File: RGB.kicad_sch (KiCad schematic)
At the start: 36 parts

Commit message: Made the project portable
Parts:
- CRGB1, CRGB10, CRGB11, CRGB12, CRGB13, CRGB14, CRGB15, CRGB16, CRGB17, CRGB18, CRGB2, CRGB3, CRGB4, CRGB5, CRGB6, CRGB7, CRGB8, CRGB9: footprint locallib:C_0603 -> KBD8X_MK2_Components:C_0603; symbol Device:C_Small -> KBD8X_MK2_Components:C_Small
- RGB1, RGB10, RGB11, RGB12, RGB13, RGB14, RGB15, RGB16, RGB17, RGB18, RGB2, RGB3, RGB4, RGB5, RGB6, RGB7, RGB8, RGB9: footprint locallib:LED_WS2812B-PLCC4 -> LED_SMD:LED_WS2812B_PLCC4_5.0x5.0mm_P3.2mm; symbol LED:WS2812B -> KBD8X_MK2_Components:WS2812B

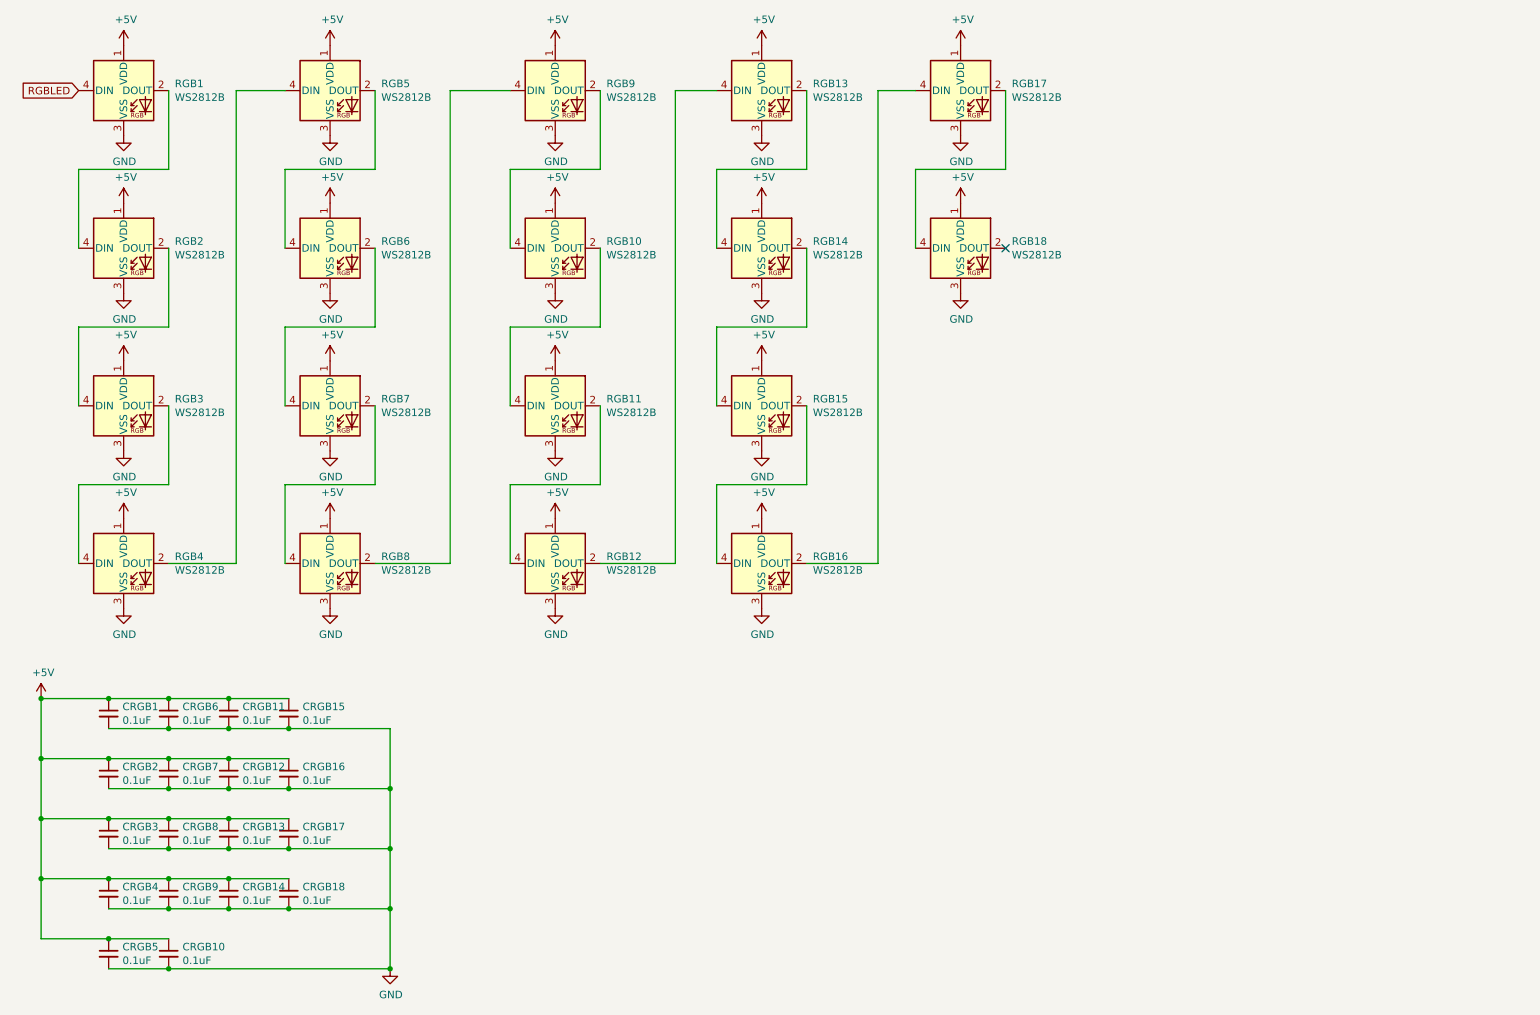
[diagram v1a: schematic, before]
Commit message: Rearrenged schematics items
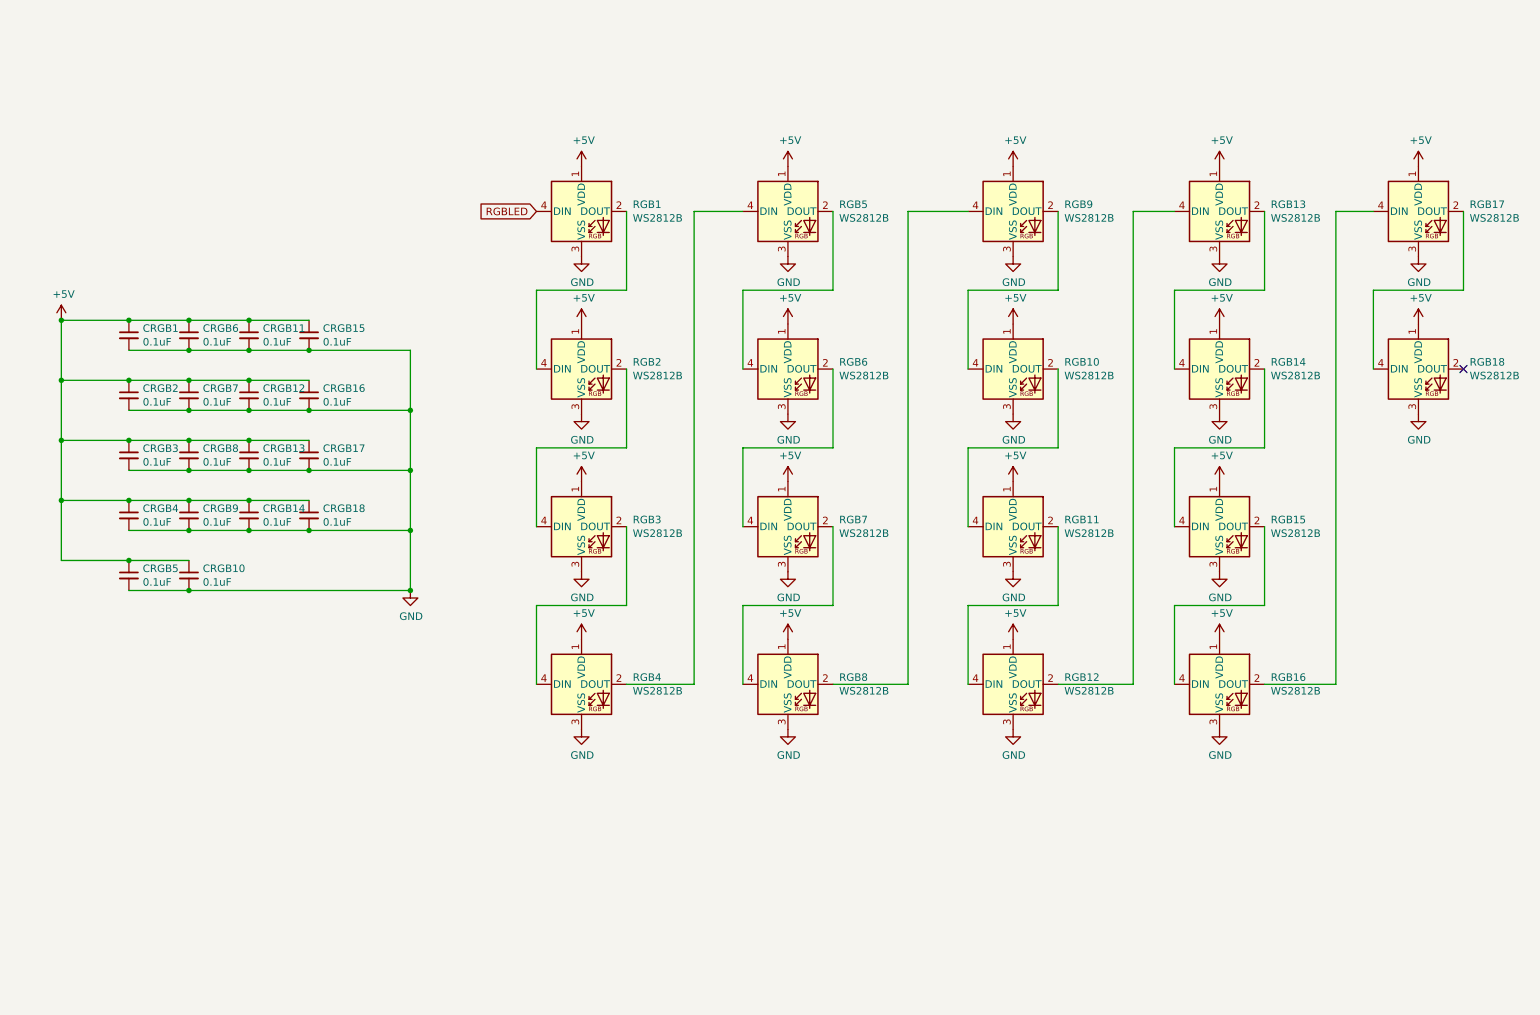
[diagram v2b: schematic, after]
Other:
- moved on the sheet: CRGB1, CRGB10, CRGB11, CRGB12, CRGB13, CRGB14, CRGB15, CRGB16, CRGB17, CRGB18, CRGB2, CRGB3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

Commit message: Added 3U and 10U footprints to the PCB
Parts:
- RGB1, RGB10, RGB11, RGB12, RGB13, RGB14, RGB15, RGB16, RGB17, RGB18, RGB2, RGB3, RGB4, RGB5, RGB6, RGB7, RGB8, RGB9: footprint LED_SMD:LED_WS2812B_PLCC4_5.0x5.0mm_P3.2mm -> KBD8X_MK2_Components:LED_WS2812B-PLCC4
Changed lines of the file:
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@@
       (effects (font (size 1.27 1.27)) (justify left))
     )
-    (property "Footprint" "LED_SMD:LED_WS2812B_PLCC4_5.0x5.0mm_P3.2mm" (id 2) (at 114.935 63.627 0)
+    (property "Footprint" "KBD8X_MK2_Components:LED_WS2812B-PLCC4" (id 2) (at 114.935 63.627 0)
       (effects (font (size 1.27 1.27)) (justify left top) hide)
     )
@@
       (effects (font (size 1.27 1.27)) (justify left))
     )
-    (property "Footprint" "LED_SMD:LED_WS2812B_PLCC4_5.0x5.0mm_P3.2mm" (id 2) (at 114.935 90.297 0)
+    (property "Footprint" "KBD8X_MK2_Components:LED_WS2812B-PLCC4" (id 2) (at 114.935 90.297 0)
       (effects (font (size 1.27 1.27)) (justify left top) hide)
     )
@@
       (effects (font (size 1.27 1.27)) (justify left))
     )
-    (property "Footprint" "LED_SMD:LED_WS2812B_PLCC4_5.0x5.0mm_P3.2mm" (id 2) (at 114.935 116.967 0)
+    (property "Footprint" "KBD8X_MK2_Components:LED_WS2812B-PLCC4" (id 2) (at 114.935 116.967 0)
       (effects (font (size 1.27 1.27)) (justify left top) hide)
     )
@@
       (effects (font (size 1.27 1.27)) (justify left))
     )
-    (property "Footprint" "LED_SMD:LED_WS2812B_PLCC4_5.0x5.0mm_P3.2mm" (id 2) (at 114.935 143.637 0)
+    (property "Footprint" "KBD8X_MK2_Components:LED_WS2812B-PLCC4" (id 2) (at 114.935 143.637 0)
       (effects (font (size 1.27 1.27)) (justify left top) hide)
     )
@@
       (effects (font (size 1.27 1.27)) (justify left))
     )
-    (property "Footprint" "LED_SMD:LED_WS2812B_PLCC4_5.0x5.0mm_P3.2mm" (id 2) (at 149.86 63.627 0)
+    (property "Footprint" "KBD8X_MK2_Components:LED_WS2812B-PLCC4" (id 2) (at 149.86 63.627 0)
       (effects (font (size 1.27 1.27)) (justify left top) hide)
     )
@@
       (effects (font (size 1.27 1.27)) (justify left))
     )
-    (property "Footprint" "LED_SMD:LED_WS2812B_PLCC4_5.0x5.0mm_P3.2mm" (id 2) (at 149.86 90.297 0)
+    (property "Footprint" "KBD8X_MK2_Components:LED_WS2812B-PLCC4" (id 2) (at 149.86 90.297 0)
       (effects (font (size 1.27 1.27)) (justify left top) hide)
     )
@@
       (effects (font (size 1.27 1.27)) (justify left))
     )
-    (property "Footprint" "LED_SMD:LED_WS2812B_PLCC4_5.0x5.0mm_P3.2mm" (id 2) (at 149.86 116.967 0)
+    (property "Footprint" "KBD8X_MK2_Components:LED_WS2812B-PLCC4" (id 2) (at 149.86 116.967 0)
       (effects (font (size 1.27 1.27)) (justify left top) hide)
     )
@@
       (effects (font (size 1.27 1.27)) (justify left))
     )
-    (property "Footprint" "LED_SMD:LED_WS2812B_PLCC4_5.0x5.0mm_P3.2mm" (id 2) (at 149.86 143.637 0)
+    (property "Footprint" "KBD8X_MK2_Components:LED_WS2812B-PLCC4" (id 2) (at 149.86 143.637 0)
       (effects (font (size 1.27 1.27)) (justify left top) hide)
     )
@@
       (effects (font (size 1.27 1.27)) (justify left))
     )
-    (property "Footprint" "LED_SMD:LED_WS2812B_PLCC4_5.0x5.0mm_P3.2mm" (id 2) (at 187.96 63.627 0)
+    (property "Footprint" "KBD8X_MK2_Components:LED_WS2812B-PLCC4" (id 2) (at 187.96 63.627 0)
       (effects (font (size 1.27 1.27)) (justify left top) hide)
     )
@@
       (effects (font (size 1.27 1.27)) (justify left))
     )
-    (property "Footprint" "LED_SMD:LED_WS2812B_PLCC4_5.0x5.0mm_P3.2mm" (id 2) (at 187.96 90.297 0)
+    (property "Footprint" "KBD8X_MK2_Components:LED_WS2812B-PLCC4" (id 2) (at 187.96 90.297 0)
       (effects (font (size 1.27 1.27)) (justify left top) hide)
     )
@@
       (effects (font (size 1.27 1.27)) (justify left))
     )
-    (property "Footprint" "LED_SMD:LED_WS2812B_PLCC4_5.0x5.0mm_P3.2mm" (id 2) (at 187.96 116.967 0)
+    (property "Footprint" "KBD8X_MK2_Components:LED_WS2812B-PLCC4" (id 2) (at 187.96 116.967 0)
       (effects (font (size 1.27 1.27)) (justify left top) hide)
     )
@@
       (effects (font (size 1.27 1.27)) (justify left))
     )
-    (property "Footprint" "LED_SMD:LED_WS2812B_PLCC4_5.0x5.0mm_P3.2mm" (id 2) (at 187.96 143.637 0)
+    (property "Footprint" "KBD8X_MK2_Components:LED_WS2812B-PLCC4" (id 2) (at 187.96 143.637 0)
       (effects (font (size 1.27 1.27)) (justify left top) hide)
     )
@@
       (effects (font (size 1.27 1.27)) (justify left))
     )
-    (property "Footprint" "LED_SMD:LED_WS2812B_PLCC4_5.0x5.0mm_P3.2mm" (id 2) (at 222.885 63.627 0)
+    (property "Footprint" "KBD8X_MK2_Components:LED_WS2812B-PLCC4" (id 2) (at 222.885 63.627 0)
       (effects (font (size 1.27 1.27)) (justify left top) hide)
     )
@@
       (effects (font (size 1.27 1.27)) (justify left))
     )
-    (property "Footprint" "LED_SMD:LED_WS2812B_PLCC4_5.0x5.0mm_P3.2mm" (id 2) (at 222.885 90.297 0)
+    (property "Footprint" "KBD8X_MK2_Components:LED_WS2812B-PLCC4" (id 2) (at 222.885 90.297 0)
       (effects (font (size 1.27 1.27)) (justify left top) hide)
     )
@@
       (effects (font (size 1.27 1.27)) (justify left))
     )
-    (property "Footprint" "LED_SMD:LED_WS2812B_PLCC4_5.0x5.0mm_P3.2mm" (id 2) (at 222.885 116.967 0)
+    (property "Footprint" "KBD8X_MK2_Components:LED_WS2812B-PLCC4" (id 2) (at 222.885 116.967 0)
       (effects (font (size 1.27 1.27)) (justify left top) hide)
     )
@@
       (effects (font (size 1.27 1.27)) (justify left))
     )
-    (property "Footprint" "LED_SMD:LED_WS2812B_PLCC4_5.0x5.0mm_P3.2mm" (id 2) (at 222.885 143.637 0)
+    (property "Footprint" "KBD8X_MK2_Components:LED_WS2812B-PLCC4" (id 2) (at 222.885 143.637 0)
       (effects (font (size 1.27 1.27)) (justify left top) hide)
     )
@@
       (effects (font (size 1.27 1.27)) (justify left))
     )
-    (property "Footprint" "LED_SMD:LED_WS2812B_PLCC4_5.0x5.0mm_P3.2mm" (id 2) (at 256.54 63.627 0)
+    (property "Footprint" "KBD8X_MK2_Components:LED_WS2812B-PLCC4" (id 2) (at 256.54 63.627 0)
       (effects (font (size 1.27 1.27)) (justify left top) hide)
     )
@@
       (effects (font (size 1.27 1.27)) (justify left))
     )
-    (property "Footprint" "LED_SMD:LED_WS2812B_PLCC4_5.0x5.0mm_P3.2mm" (id 2) (at 256.54 90.297 0)
-      (effects (font (size 1.27 1.27)) (justify left top) hide)
-    )
+    (property "Footprint" "KBD8X_MK2_Components:LED_WS2812B-PLCC4" (id 2) (at 256.54 90.297 0)
+      (effects (font (size 1.27 1.27)) (justify left top) hide)
+    )
